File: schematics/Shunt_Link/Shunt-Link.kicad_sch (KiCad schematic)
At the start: 31 parts, among them IC1 AD8221TRMZ-EP, IC2 AD8221TRMZ-EP, IC3 AD8221TRMZ-EP, IC4 AD8221TRMZ-EP, J1 PCIE-036-02-X-D-TH, J2 Conn_01x05_Socket, J3 Conn_01x05_Socket, U1 LM7805S/NOPB, U2 ADP7158ARDZ-3.3-R7

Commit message: Modifications to Shunt Link
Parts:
- removed C1, C5, C7: 0.1 uF, Capacitor_SMD:C_1210_3225Metric, symbol Device:C
- removed C10, C9: 1uF, symbol Device:C_Small
- removed C11, C12, C13: 10uF, symbol Device:C_Small
- removed C2, C6, C8: 10 uF, Capacitor_SMD:C_1210_3225Metric, symbol Device:C_US
- removed IC1: AD8221TRMZ-EP, Link_Footprints:AD8221TRMZ-EP, symbol Link_Components:AD8221TRMZ-EP
- removed J2, J3: Conn_01x05_Socket, Link_Footprints:Phoenix_Contact_MSTBA,5-LR, symbol Connector:Conn_01x05_Socket
- removed R1: 6.25, Resistor_SMD:R_0805_2012Metric, symbol Device:R_US
- removed Rg_1, Rg_4: 499, Resistor_SMD:R_0805_2012Metric, symbol Device:R_Small_US
- removed U1: LM7805S/NOPB, KTT0003B_N, symbol Link_Components:LM7805S_NOPB
- removed U2: ADP7158ARDZ-3.3-R7, ADP7158ARDZ-3.3-R7_ADI, symbol Link_Components:ADP7158ARDZ-3.3-R7
- added IC3: AD8221TRMZ-EP, Link_Footprints:AD8221TRMZ-EP, symbol Link_Components:AD8221TRMZ-EP
- added J2, J3: Conn_02x03_Odd_Even, Link_Footprints:1818517, symbol Connector_Generic:Conn_02x03_Odd_Even
- added R10, R11, R12, R4, R5: R, Resistor_SMD:R_2512_6332Metric, symbol Device:R_US
- added R7: R_{g3}, Resistor_SMD:R_2512_6332Metric, symbol Device:R_Small_US
- added R9: R_{g4}, Resistor_SMD:R_2512_6332Metric, symbol Device:R_Small_US
- added TP1: S1, Link_Footprints:KEYSTONE_5017, symbol Connector:TestPoint
- added TP2: T1, Link_Footprints:KEYSTONE_5017, symbol Connector:TestPoint
- added TP3: S2, Link_Footprints:KEYSTONE_5017, symbol Connector:TestPoint
- added TP4: T2, Link_Footprints:KEYSTONE_5017, symbol Connector:TestPoint
- added TP5: GND, Link_Footprints:KEYSTONE_5017, symbol Connector:TestPoint
- J1: footprint (none) -> Connector_PCBEdge:BUS_PCIexpress_x1
- R1: renamed from Rg_3; value 499 -> R_{g1}; footprint Resistor_SMD:R_0805_2012Metric -> Resistor_SMD:R_2512_6332Metric
- R2: renamed from R7; value 6.25 -> R_{shunt}; footprint Resistor_SMD:R_0805_2012Metric -> Resistor_SMD:R_2512_6332Metric
- R3: renamed from Rg_2; value 499 -> R_{g2}; footprint Resistor_SMD:R_0805_2012Metric -> Resistor_SMD:R_2512_6332Metric
- R6: renamed from R2; value 6.25 -> R; footprint Resistor_SMD:R_0805_2012Metric -> Resistor_SMD:R_2512_6332Metric
- R8: value 6.25 -> R_{shunt}; footprint Resistor_SMD:R_0805_2012Metric -> Resistor_SMD:R_2512_6332Metric
- renumbered C3 to C1, C4 to C2, IC3 to IC1
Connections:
- net +5V is gone; now on net S_{2out}: L1.5 (INB)
- net V_sens is gone; now on net S_{2test}: L1.4 (OUTB)
- net +12V: now also R6.1, J2.1 (Pin_1), J2.4 (Pin_4), J3.1 (Pin_1), J3.4 (Pin_4), R12.1; no longer IC2.8 (+VS), IC4.8 (+VS)
- net +2V5: now also IC3.6 (REF); no longer IC2.6 (REF), IC4.6 (REF)
- net GND: now also IC3.4 (+IN), IC3.5 (-VS), J2.6 (Pin_6), J3.6 (Pin_6), R10.2, R11.2, R4.2, R5.2, TP5.1; no longer IC2.4 (+IN), IC4.4 (+IN), R6.2
- net S_{1+}: now also J2.2 (Pin_2)
- net S_{1out}: now also J1.B4, L1.1 (INA); no longer J1.B1, L1.10 (IND)
- net S_{1test}: now also L1.2 (OUTA), TP1.1; no longer L1.9 (OUTD)
- net S_{2+}: now also R8.1, IC3.1 (-IN), J3.2 (Pin_2)
- net S_{2out}: now also J1.B1, IC3.7 (VOUT); no longer J1.B3, L1.6 (INC)
- net S_{2test}: now also TP3.1; no longer L1.7 (OUTC)
- net T_{1out}: now also J1.B3, L1.9 (OUTD); no longer J1.B2
- net T_{2out}: now also J1.B2, L1.7 (OUTC); no longer J1.B4
- net at IC4.2 (RG_1): now also R9.1
- net at IC4.3 (RG_2): now also R9.2
- net T_{1+} renamed T_{1-}
- net T_{1-}: now also J2.3 (Pin_3), R4.1; no longer R6.1
- net T_{2+} renamed T_{2-}
- net T_{2-}: now also J3.3 (Pin_3), R10.1; no longer R8.1
- new net: IC3.2 (RG_1), R7.1
- new net: IC3.3 (RG_2), R7.2
- new net: IC2.4 (+IN), R5.1, R6.2
- new net: IC4.4 (+IN), R11.1, R12.2
- new net T_{1test}: L1.10 (IND), TP2.1
- new net T_{2test}: L1.6 (INC), TP4.1
- new net V_{ref}: IC2.6 (REF), IC4.6 (REF)
- no-connect marks 34 -> 32
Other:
- note removed: "Power Regulation"
- moved on the sheet: C1, C2, IC2, J1, R3, R6

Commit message: Start rev2
- Smaller resistors
- Swap filled zones (GND should be top layer)
- Extend filled zones to edges
- Give each in-amp capacitors
- Fix IC trace angles (Should only come out at 90 degrees)
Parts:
- added C3, C5, C7: 0.1 uF, Capacitor_SMD:C_0603_1608Metric, symbol Device:C
- added C4, C6, C8: 10 uF, Capacitor_SMD:C_0603_1608Metric, symbol Device:C_US
- C1, C2: footprint Capacitor_SMD:C_1210_3225Metric -> Capacitor_SMD:C_0603_1608Metric
- R1, R10, R11, R12, R2, R3, R4, R5, R6, R7, R8, R9: footprint Resistor_SMD:R_2512_6332Metric -> Resistor_SMD:R_0805_2012Metric
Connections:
- net +12V: now also IC2.8 (+VS), IC3.8 (+VS), IC4.8 (+VS), C3.1, C4.1, C5.1, C6.1, C7.1, C8.1
- net GND: now also C3.2, C4.2, C5.2, C6.2, C7.2, C8.2

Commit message: Update libraries to one lib for all projects
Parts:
- IC1, IC2, IC3, IC4: footprint Link_Footprints:AD8221TRMZ-EP -> Link Footprints:AD8221TRMZ; symbol Link_Components:AD8221TRMZ-EP -> Link_Components:AD8221TRMZ
- J2, J3: footprint Link_Footprints:1818517 -> Link Footprints:PC-1818517
- L1: footprint Link_Footprints:AD8244ARMZ -> Link Footprints:AD8244ARMZ
- TP1, TP2, TP3, TP4, TP5: footprint Link_Footprints:KEYSTONE_5017 -> Link Footprints:Keystone_5017
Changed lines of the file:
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@@
 	)
 	(symbol
-		(lib_id "Link_Components:AD8221TRMZ-EP")
+		(lib_id "Link_Components:AD8221TRMZ")
 		(at 119.38 95.25 0)
 		(unit 1)
@@
 			)
 		)
-		(property "Footprint" "Link_Footprints:AD8221TRMZ-EP"
+		(property "Footprint" "Link Footprints:AD8221TRMZ"
 			(at 143.51 190.17 0)
 			(effects
@@
 	)
 	(symbol
-		(lib_id "Link_Components:AD8221TRMZ-EP")
+		(lib_id "Link_Components:AD8221TRMZ")
 		(at 121.92 64.77 0)
 		(unit 1)
@@
 			)
 		)
-		(property "Footprint" "Link_Footprints:AD8221TRMZ-EP"
+		(property "Footprint" "Link Footprints:AD8221TRMZ"
 			(at 146.05 159.69 0)
 			(effects
@@
 			)
 		)
-		(property "Footprint" "Link_Footprints:KEYSTONE_5017"
+		(property "Footprint" "Link Footprints:Keystone_5017"
 			(at 228.6 100.33 0)
 			(effects
@@
 			)
 		)
-		(property "Footprint" "Link_Footprints:KEYSTONE_5017"
+		(property "Footprint" "Link Footprints:Keystone_5017"
 			(at 228.6 125.73 0)
 			(effects
@@
 			)
 		)
-		(property "Footprint" "Link_Footprints:KEYSTONE_5017"
+		(property "Footprint" "Link Footprints:Keystone_5017"
 			(at 228.6 119.38 0)
 			(effects
@@
 	)
 	(symbol
-		(lib_id "Link_Components:AD8221TRMZ-EP")
+		(lib_id "Link_Components:AD8221TRMZ")
 		(at 121.92 125.73 0)
 		(unit 1)
@@
 			)
 		)
-		(property "Footprint" "Link_Footprints:AD8221TRMZ-EP"
+		(property "Footprint" "Link Footprints:AD8221TRMZ"
 			(at 146.05 220.65 0)
 			(effects
@@
 			)
 		)
-		(property "Footprint" "Link_Footprints:KEYSTONE_5017"
+		(property "Footprint" "Link Footprints:Keystone_5017"
 			(at 228.6 113.03 0)
 			(effects
@@
 			)
 		)
-		(property "Footprint" "Link_Footprints:1818517"
+		(property "Footprint" "Link Footprints:PC-1818517"
 			(at 34.29 34.29 0)
 			(effects
@@
 			)
 		)
-		(property "Footprint" "Link_Footprints:KEYSTONE_5017"
+		(property "Footprint" "Link Footprints:Keystone_5017"
 			(at 228.6 106.68 0)
 			(effects
@@
 			)
 		)
-		(property "Footprint" "Link_Footprints:1818517"
+		(property "Footprint" "Link Footprints:PC-1818517"
 			(at 34.29 52.07 0)
 			(effects
@@
 			)
 		)
-		(property "Footprint" "Link_Footprints:AD8244ARMZ"
+		(property "Footprint" "Link Footprints:AD8244ARMZ"
 			(at 246.38 230.81 0)
 			(effects
@@
 	)
 	(symbol
-		(lib_id "Link_Components:AD8221TRMZ-EP")
+		(lib_id "Link_Components:AD8221TRMZ")
 		(at 119.38 34.29 0)
 		(unit 1)
@@
 			)
 		)
-		(property "Footprint" "Link_Footprints:AD8221TRMZ-EP"
+		(property "Footprint" "Link Footprints:AD8221TRMZ"
 			(at 143.51 129.21 0)
 			(effects

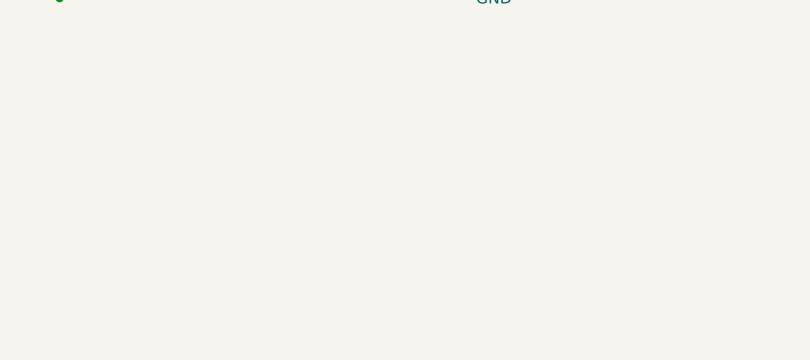
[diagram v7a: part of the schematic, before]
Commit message: feat(gain-link): Started a signal chain sub sheet
Signed-off-by: Andrew Balmos <andrew@balmos.org>
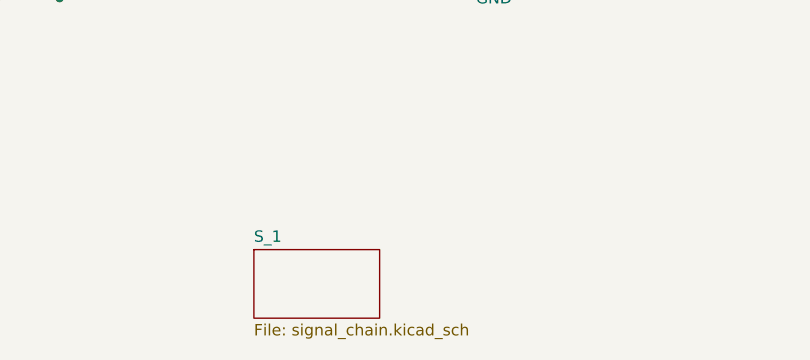
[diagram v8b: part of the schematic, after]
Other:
- added sheet S_1 (signal_chain.kicad_sch)
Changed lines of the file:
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@@
+		)
+	)
+	(sheet
+		(at 125.73 166.37)
+		(size 13.97 7.62)
+		(exclude_from_sim no)
+		(in_bom yes)
+		(on_board yes)
+		(dnp no)
+		(fields_autoplaced yes)
+		(stroke
+			(width 0.1524)
+			(type solid)
+		)
+		(fill
+			(color 0 0 0 0.0000)
+		)
+		(property "Sheetname" "S_1"
+			(at 125.73 165.6584 0)
+			(effects
+				(font
+					(size 1.27 1.27)
+				)
+				(justify left bottom)
+			)
+		)
+		(property "Sheetfile" "signal_chain.kicad_sch"
+			(at 125.73 174.5746 0)
+			(effects
+				(font
+					(size 1.27 1.27)
+				)
+				(justify left top)
+			)
+		)
+		(instances
+			(project "Shunt-Link"
+				(path "/044df771-0288-4dc4-a604-257e905d1378"
+					(page "2")
+				)
+			)
 		)
 	)
